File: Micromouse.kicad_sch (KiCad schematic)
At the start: 71 parts, among them J1 JST Connector, J2 JST Connector, J3 Left Header, J4 Right Header, J6 STLink Connector, Q1 Phototransistor, Q2 Phototransistor, Q3 Phototransistor, Q4 Phototransistor, SW1 Button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

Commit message: added project specific symbols and footprints
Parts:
- D1, D2, D3: footprint (none) -> LED_LTST-C170GKT:LTST-C170GKT
- J3, J4: footprint (none) -> Connector_PinHeader_1.27mm:PinHeader_1x04_P1.27mm_Vertical
- J6: footprint (none) -> Connector_PinSocket_2.54mm:PinSocket_1x04_P2.54mm_Vertical
- S1: footprint EG1218:SW_EG1218 -> Power_Switch_EG1218:SW_EG1218
- SW1: footprint Button_FP_FSM4JSMA:TE_FSM4JSMA -> Button_Switch_SMD:SW_SPST_B3S-1000
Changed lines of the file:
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@@
 			)
 		)
-		(property "Footprint" "Button_FP_FSM4JSMA:TE_FSM4JSMA"
+		(property "Footprint" "Button_Switch_SMD:SW_SPST_B3S-1000"
 			(at 40.64 163.83 0)
 			(effects
@@
 			)
 		)
-		(property "Footprint" "EG1218:SW_EG1218"
+		(property "Footprint" "Power_Switch_EG1218:SW_EG1218"
 			(at 21.59 111.76 0)
 			(effects
@@
 			)
 		)
-		(property "Footprint" ""
+		(property "Footprint" "LED_LTST-C170GKT:LTST-C170GKT"
 			(at 245.11 101.6 0)
 			(effects
@@
 			)
 		)
-		(property "Footprint" ""
+		(property "Footprint" "Connector_PinHeader_1.27mm:PinHeader_1x04_P1.27mm_Vertical"
 			(at 120.65 78.74 0)
 			(effects
@@
 			)
 		)
-		(property "Footprint" ""
+		(property "Footprint" "LED_LTST-C170GKT:LTST-C170GKT"
 			(at 115.57 161.29 0)
 			(effects
@@
 			)
 		)
-		(property "Footprint" ""
+		(property "Footprint" "Connector_PinHeader_1.27mm:PinHeader_1x04_P1.27mm_Vertical"
 			(at 139.7 76.2 0)
 			(effects
@@
 			)
 		)
-		(property "Footprint" ""
+		(property "Footprint" "LED_LTST-C170GKT:LTST-C170GKT"
 			(at 246.38 99.06 0)
 			(effects
@@
 			)
 		)
-		(property "Footprint" ""
+		(property "Footprint" "Connector_PinSocket_2.54mm:PinSocket_1x04_P2.54mm_Vertical"
 			(at 90.17 161.29 0)
 			(effects

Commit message: fixed errors
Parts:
- J3, J4: footprint Connector_PinHeader_1.27mm:PinHeader_1x04_P1.27mm_Vertical -> Connector_PinHeader_1.27mm:PinHeader_1x06_P1.27mm_Vertical
- SW1: footprint Button_Switch_SMD:SW_SPST_B3S-1000 -> Button_FSM4JSMA:TE_FSM4JSMA
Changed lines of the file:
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@@
 			)
 		)
-		(property "Footprint" "Button_Switch_SMD:SW_SPST_B3S-1000"
+		(property "Footprint" "Button_FSM4JSMA:TE_FSM4JSMA"
 			(at 40.64 163.83 0)
 			(effects
@@
 			)
 		)
-		(property "Footprint" "Connector_PinHeader_1.27mm:PinHeader_1x04_P1.27mm_Vertical"
+		(property "Footprint" "Connector_PinHeader_1.27mm:PinHeader_1x06_P1.27mm_Vertical"
 			(at 120.65 78.74 0)
 			(effects
@@
 			)
 		)
-		(property "Footprint" "Connector_PinHeader_1.27mm:PinHeader_1x04_P1.27mm_Vertical"
+		(property "Footprint" "Connector_PinHeader_1.27mm:PinHeader_1x06_P1.27mm_Vertical"
 			(at 139.7 76.2 0)
 			(effects

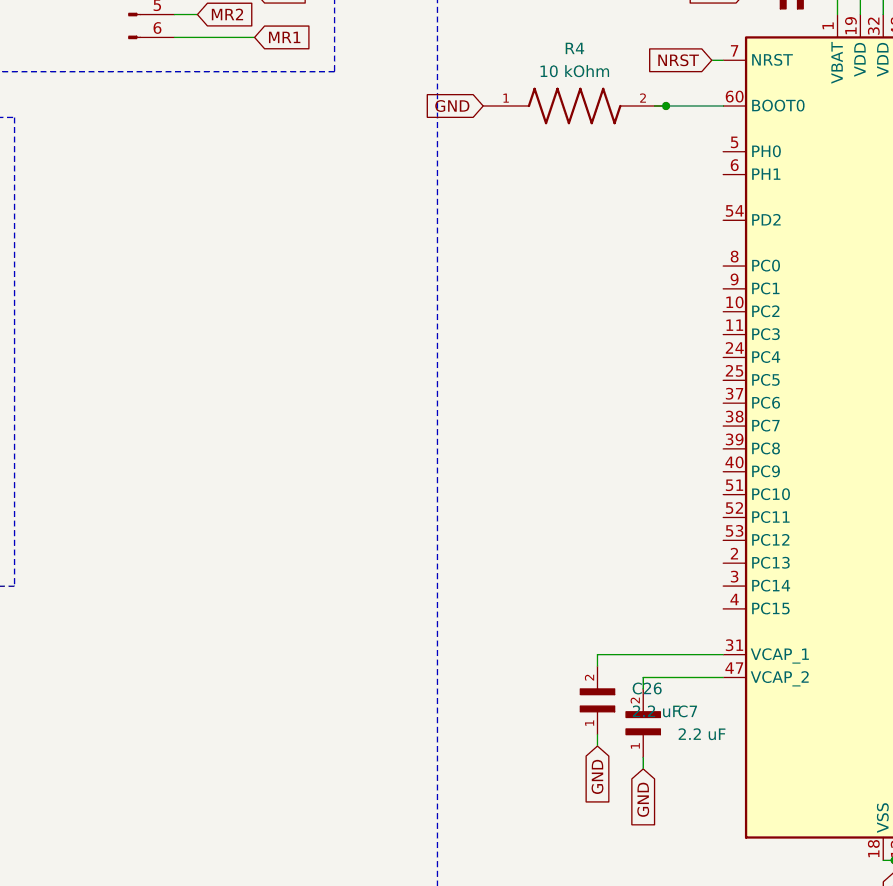
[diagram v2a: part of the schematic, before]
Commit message: Reorganized components
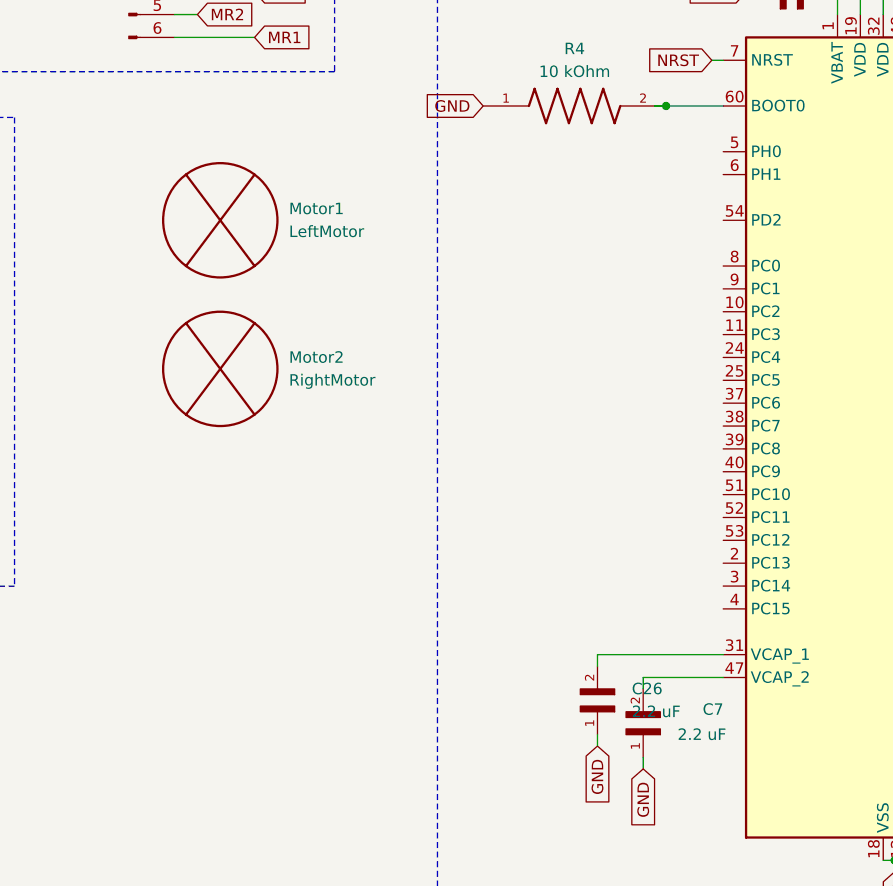
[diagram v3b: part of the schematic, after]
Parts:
- added Motor1: LeftMotor, Pololu_Motor:Pololu_Motor, symbol pololu_motor:Pololu_Motor
- added Motor2: RightMotor, Pololu_Motor:Pololu_Motor, symbol pololu_motor:Pololu_Motor
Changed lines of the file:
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@@
 	)
 	(symbol
+		(lib_id "pololu_motor:Pololu_Motor")
+		(at 149.86 128.27 0)
+		(unit 1)
+		(exclude_from_sim no)
+		(in_bom yes)
+		(on_board yes)
+		(dnp no)
+		(fields_autoplaced yes)
+		(property "Reference" "Motor2"
+			(at 157.48 119.3799 0)
+			(effects
+				(font
+					(size 1.27 1.27)
+				)
+				(justify left)
+			)
+		)
+		(property "Value" "RightMotor"
+			(at 157.48 121.9199 0)
+			(effects
+				(font
+					(size 1.27 1.27)
+				)
+				(justify left)
+			)
+		)
+		(property "Footprint" "Pololu_Motor:Pololu_Motor"
+			(at 149.86 128.27 0)
+			(effects
+				(font
+					(size 1.27 1.27)
+				)
+				(hide yes)
+			)
+		)
+		(property "Datasheet" ""
+			(at 149.86 128.27 0)
+			(effects
+				(font
+					(size 1.27 1.27)
+				)
+				(hide yes)
+			)
+		)
+		(property "Description" ""
+			(at 149.86 128.27 0)
+			(effects
+				(font
+					(size 1.27 1.27)
+				)
+				(hide yes)
+			)
+		)
+		(instances
+			(project ""
+				(path "/51d021f8-4273-43ac-b1ec-f423b86f2e75"
+					(reference "Motor2")
+					(unit 1)
+				)
+			)
+		)
+	)
+	(symbol
 		(lib_id "power:VCC")
 		(at 152.4 34.29 270)
@@
 	)
 	(symbol
+		(lib_id "pololu_motor:Pololu_Motor")
+		(at 149.86 111.76 0)
+		(unit 1)
+		(exclude_from_sim no)
+		(in_bom yes)
+		(on_board yes)
+		(dnp no)
+		(fields_autoplaced yes)
+		(property "Reference" "Motor1"
+			(at 157.48 102.8699 0)
+			(effects
+				(font
+					(size 1.27 1.27)
+				)
+				(justify left)
+			)
+		)
+		(property "Value" "LeftMotor"
+			(at 157.48 105.4099 0)
+			(effects
+				(font
+					(size 1.27 1.27)
+				)
+				(justify left)
+			)
+		)
+		(property "Footprint" "Pololu_Motor:Pololu_Motor"
+			(at 149.86 111.76 0)
+			(effects
+				(font
+					(size 1.27 1.27)
+				)
+				(hide yes)
+			)
+		)
+		(property "Datasheet" ""
+			(at 149.86 111.76 0)
+			(effects
+				(font
+					(size 1.27 1.27)
+				)
+				(hide yes)
+			)
+		)
+		(property "Description" ""
+			(at 149.86 111.76 0)
+			(effects
+				(font
+					(size 1.27 1.27)
+				)
+				(hide yes)
+			)
+		)
+		(instances
+			(project ""
+				(path "/51d021f8-4273-43ac-b1ec-f423b86f2e75"
+					(reference "Motor1")
+					(unit 1)
+				)
+			)
+		)
+	)
+	(symbol
 		(lib_id "100ohm_RC0805FR-07100RL:RC0805FR-07100RL")
 		(at 358.14 213.36 0)
@@
 		(on_board yes)
 		(dnp no)
-		(fields_autoplaced yes)
 		(property "Reference" "C7"
-			(at 200.66 158.7499 90)
+			(at 203.454 158.496 90)
 			(effects
 				(font

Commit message: ir
renamed ir emitters and reformatted the pcb a little bit
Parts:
- LED1: value IR Emitter -> Left IR Emitter
- LED2: value IR Emitter -> Front Left IR Emitter
- LED3: value IR Emitter -> Front Right IR Emitter
- LED4: value IR Emitter -> Right IR Emitter
- Q1: value Phototransistor -> Left Phototransistor
- Q2: value Phototransistor -> Front Left Phototransistor
- Q3: value Phototransistor -> Front Right Phototransistor
- Q4: value Phototransistor -> Right Phototransistor
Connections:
- net PC5: no longer Q2.1, Q3.1, Q4.1, R12.2, R16.2, R20.2
- net PC9: no longer R13.1, R17.1, R9.1
- new net PA6: Q2.1, R12.2
- new net PA7: R9.1
- new net PB1: Q3.1, R16.2
- new net PB13: R17.1
- new net PB2: R13.1
- new net PC4: Q4.1, R20.2
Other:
- note added: "Front Left IR Emitter"
- note added: "Front Left IR Receiver"
- note added: "Front Right IR Emitter"
- note added: "Front Right IR Receiver"
- note added: "Left IR Emitter"
- note added: "Left IR Receiver"
- note added: "Right IR Emitter"
- note added: "Right IR Receiver"
- note removed: "IR Emitter"
- note removed: "IR Receiver"
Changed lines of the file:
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@@
 		)
 	)
-	(text "IR Receiver"
+	(text "Left IR Receiver"
 		(exclude_from_sim no)
 		(at 128.524 233.934 0)
@@
 		)
 	)
-	(text "IR Emitter"
+	(text "Right IR Emitter"
 		(exclude_from_sim no)
 		(at 337.312 8.89 0)
@@
 		)
 	)
-	(text "IR Receiver"
+	(text "Front Right IR Receiver"
 		(exclude_from_sim no)
 		(at 447.294 169.164 0)
@@
 		)
 	)
-	(text "IR Emitter"
+	(text "Left IR Emitter"
 		(exclude_from_sim no)
 		(at 18.542 209.55 0)
@@
 		)
 	)
-	(text "IR Emitter"
+	(text "Front Right IR Emitter"
 		(exclude_from_sim no)
 		(at 337.312 144.78 0)
@@
 		)
 	)
-	(text "IR Receiver"
+	(text "Right IR Receiver"
 		(exclude_from_sim no)
 		(at 447.294 33.274 0)
@@
 		)
 	)
-	(text "IR Emitter"
+	(text "Front Left IR Emitter"
 		(exclude_from_sim no)
 		(at 168.402 214.63 0)
@@
 		)
 	)
-	(text "IR Receiver"
+	(text "Front Left IR Receiver"
 		(exclude_from_sim no)
 		(at 278.384 239.014 0)
@@
 		)
 	)
-	(global_label "PC5"
+	(global_label "PA6"
 		(shape input)
 		(at 284.48 265.43 0)
@@
 		)
 		(property "Intersheetrefs" "${INTERSHEET_REFS}"
-			(at 291.2147 265.43 0)
+			(at 291.0333 265.43 0)
 			(effects
 				(font
@@
 		)
 	)
-	(global_label "PC5"
+	(global_label "PC4"
 		(shape input)
 		(at 453.39 59.69 0)
@@
 		)
 	)
-	(global_label "PC9"
+	(global_label "PA7"
 		(shape input)
 		(at 175.26 283.21 180)
@@
 		)
 		(property "Intersheetrefs" "${INTERSHEET_REFS}"
-			(at 168.5253 283.21 0)
+			(at 168.7067 283.21 0)
 			(effects
 				(font
@@
 		)
 	)
-	(global_label "PC9"
+	(global_label "PB2"
 		(shape input)
 		(at 344.17 213.36 180)
@@
 		)
 	)
-	(global_label "PC9"
+	(global_label "PB13"
 		(shape input)
 		(at 344.17 77.47 180)
@@
 		)
 		(property "Intersheetrefs" "${INTERSHEET_REFS}"
-			(at 337.4353 77.47 0)
+			(at 336.2258 77.47 0)
 			(effects
 				(font
@@
 		)
 	)
-	(global_label "PC5"
+	(global_label "PB1"
 		(shape input)
 		(at 453.39 195.58 0)
@@
 			)
 		)
-		(property "Value" "IR Emitter"
+		(property "Value" "Front Left IR Emitter"
 			(at 231.14 261.6199 90)
 			(effects
@@
 			)
 		)
-		(property "Value" "Phototransistor"
+		(property "Value" "Left Phototransistor"
 			(at 135.89 253.9999 0)
 			(effects
@@
 			)
 		)
-		(property "Value" "IR Emitter"
+		(property "Value" "Right IR Emitter"
 			(at 400.05 55.8799 90)
 			(effects
@@
 			)
 		)
-		(property "Value" "Phototransistor"
+		(property "Value" "Front Left Phototransistor"
 			(at 285.75 259.0799 0)
 			(effects
@@
 			)
 		)
-		(property "Value" "IR Emitter"
+		(property "Value" "Left IR Emitter"
 			(at 81.28 256.5399 90)
 			(effects
@@
 			)
 		)
-		(property "Value" "IR Emitter"
+		(property "Value" "Front Right IR Emitter"
 			(at 400.05 191.7699 90)
 			(effects
@@
 			)
 		)
-		(property "Value" "Phototransistor"
+		(property "Value" "Right Phototransistor"
 			(at 454.66 53.3399 0)
 			(effects
@@
 			)
 		)
-		(property "Value" "Phototransistor"
+		(property "Value" "Front Right Phototransistor"
 			(at 454.66 189.2299 0)
 			(effects

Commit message: rough draft for routing
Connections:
- net PB2 is gone; now on net PB12: R13.1
- net PA6: now also U3.22 (PA6)
- net PA7: now also U3.23 (PA7)
- net PB1: now also U3.27 (PB1)
- net PB13: now also U3.34 (PB13)
- net PC4: now also U3.24 (PC4)
- net PC5: now also U3.25 (PC5)
- net PC9: now also U3.40 (PC9)
- net at D3.1 (K): now also U3.56 (PB4); no longer U3.22 (PA6)
- net PB12: now reaches U3.33 (PB12)
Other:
- moved on the sheet: D1, D2, D3, J6, R1, R2, R23

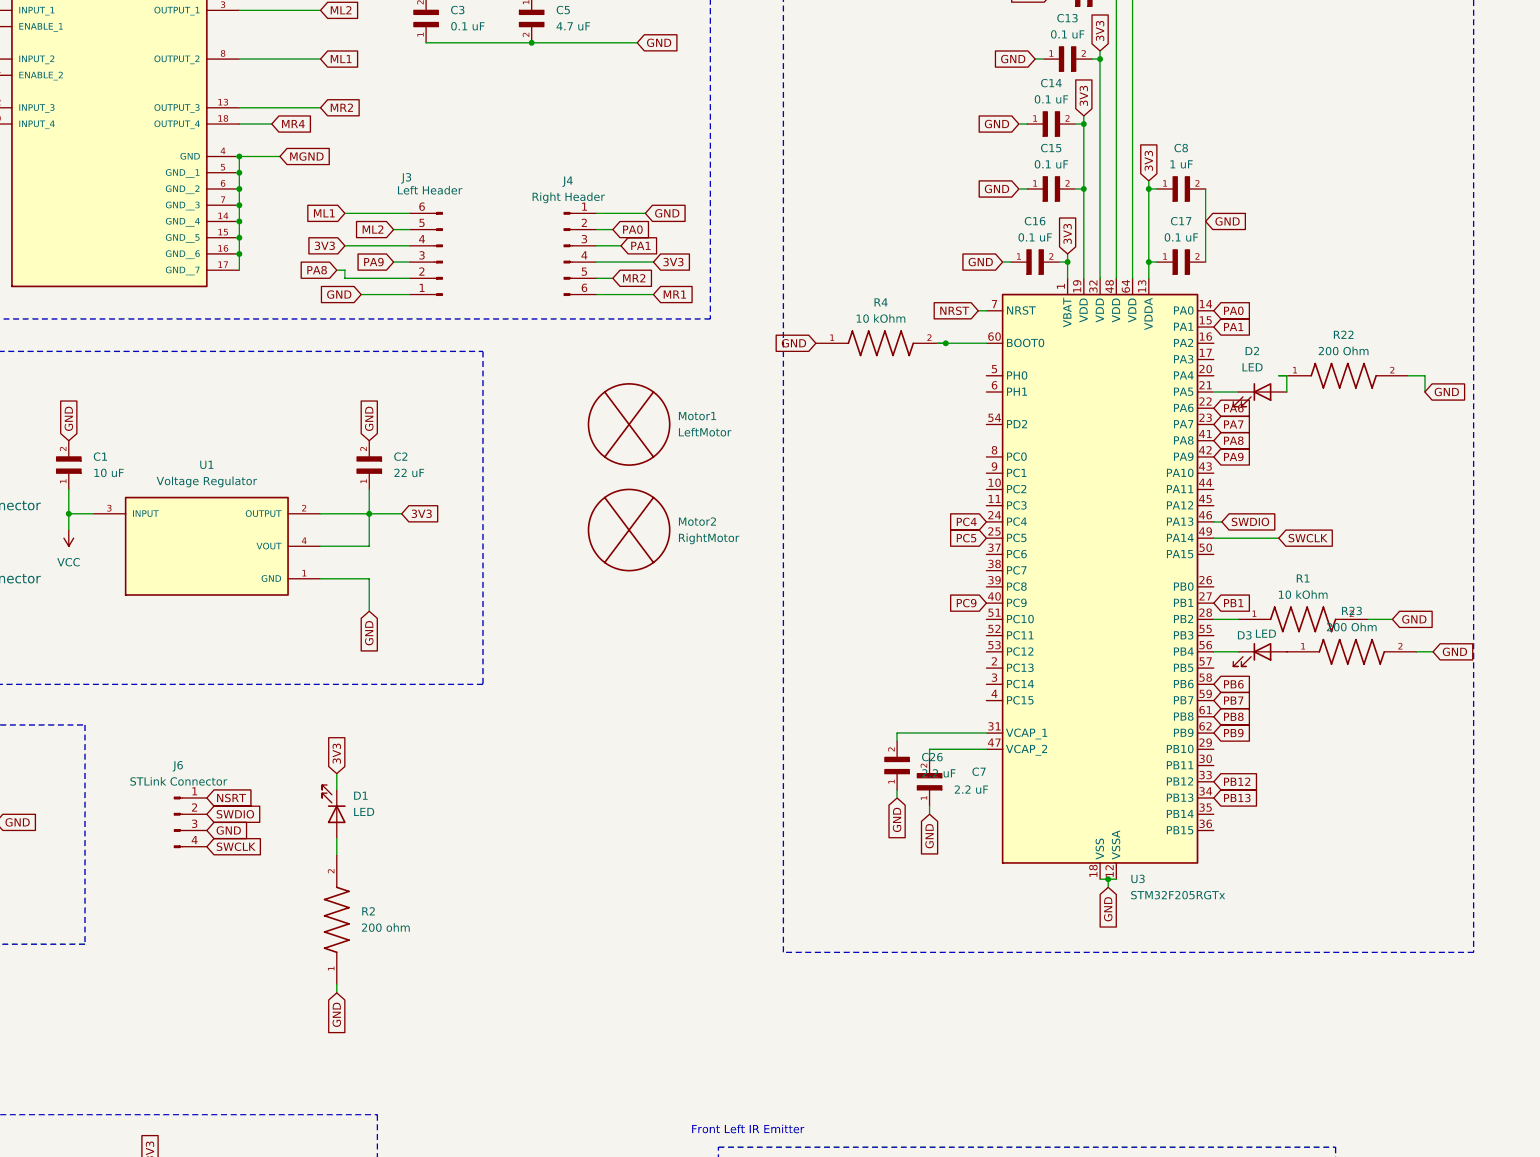
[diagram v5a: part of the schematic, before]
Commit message: finished pcb and fixed schematic
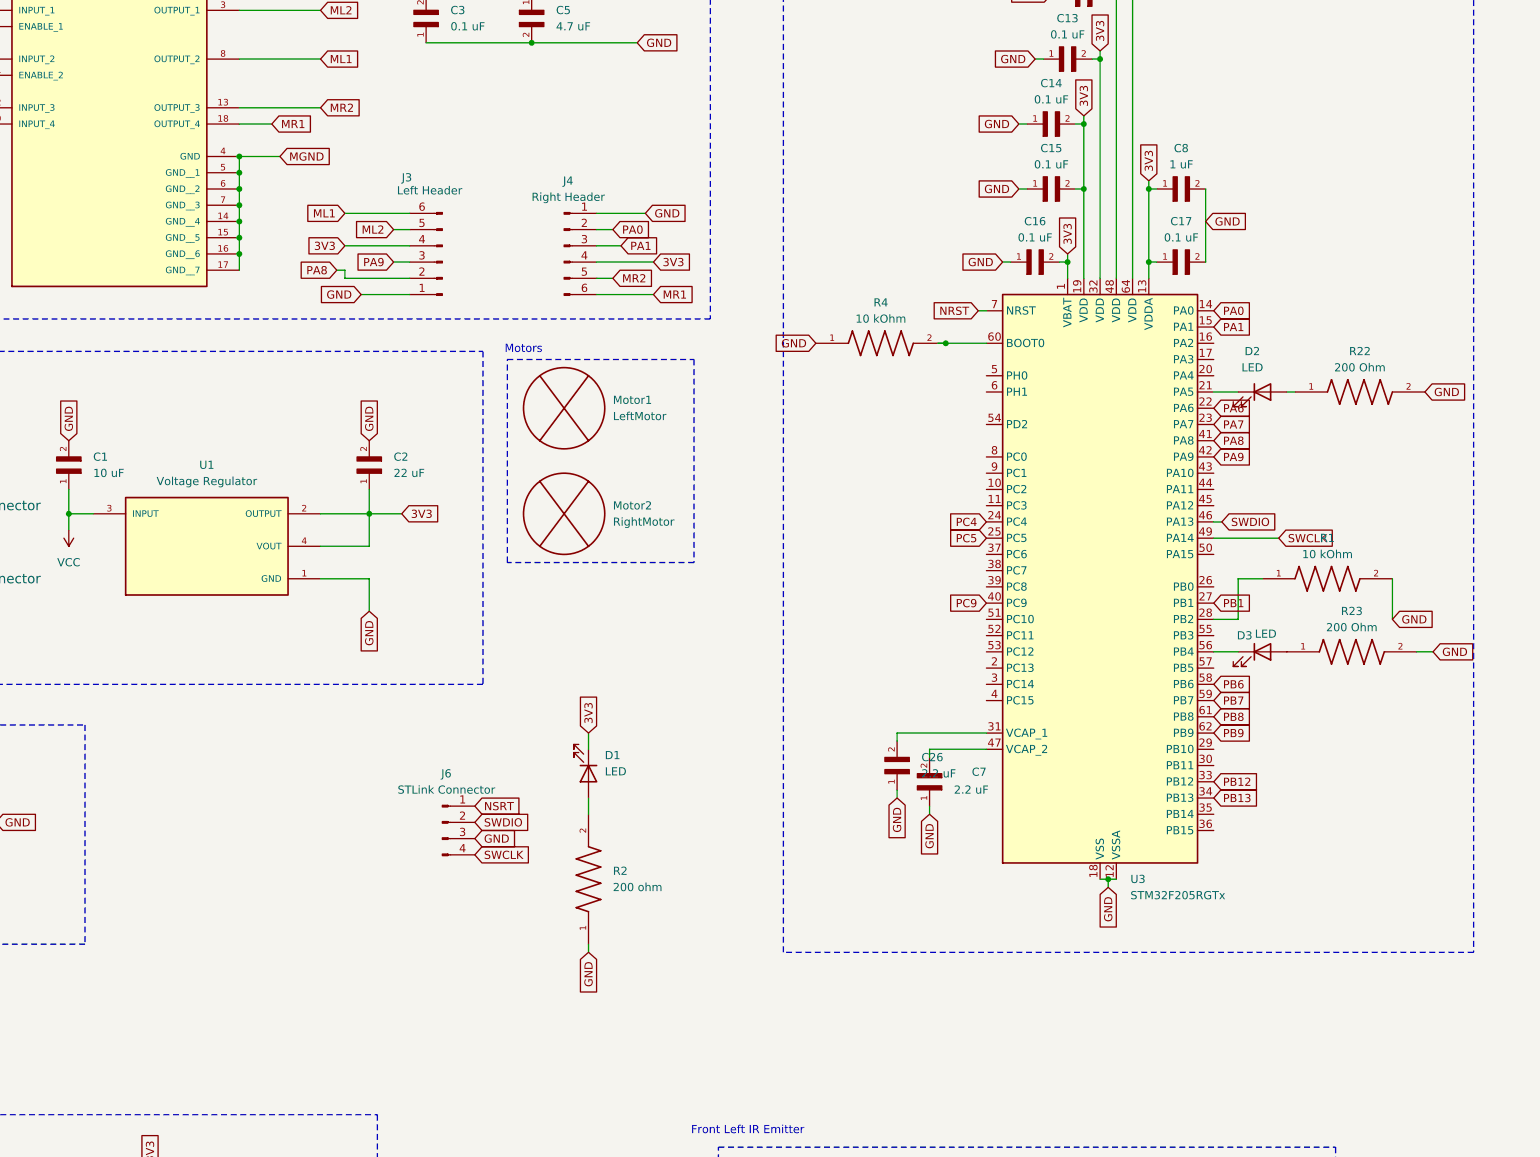
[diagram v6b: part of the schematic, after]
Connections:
- net MR4 is gone; now on net MR1: U2.18 (OUTPUT_4)
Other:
- note added: "Motors"
- moved on the sheet: D1, J6, Motor1, Motor2, R1, R2, R22

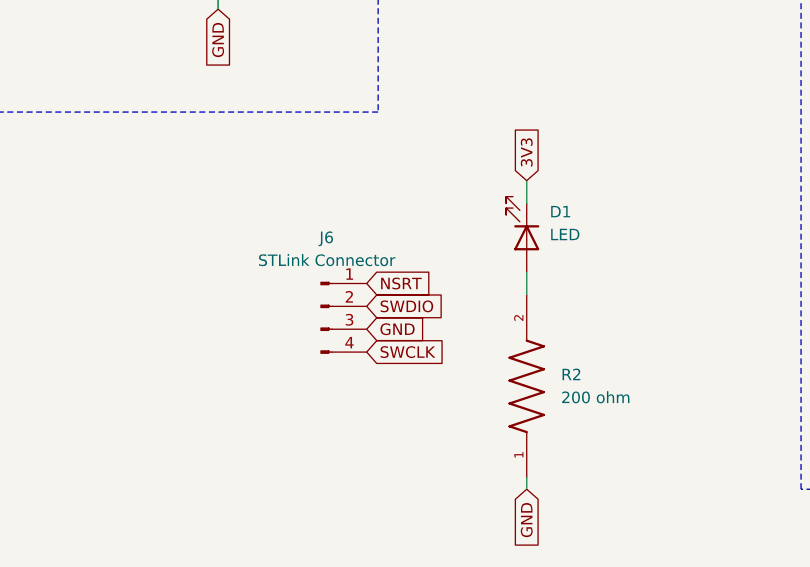
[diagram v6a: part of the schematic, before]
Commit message: fixed issues kevin pointed out
compacted the pcb, fixed nrst misspelling, re-added two copper planes
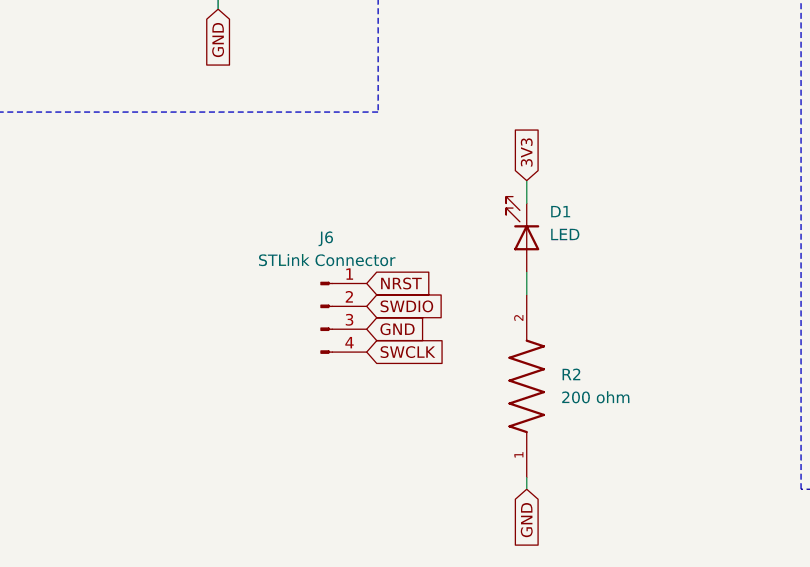
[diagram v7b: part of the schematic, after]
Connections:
- net NSRT is gone; now on net NRST: J6.1 (Pin_1)
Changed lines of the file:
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@@
 		)
 	)
-	(global_label "NSRT"
+	(global_label "NRST"
 		(shape input)
 		(at 125.73 163.83 0)
